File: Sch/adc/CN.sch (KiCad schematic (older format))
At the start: 19 parts, among them J1 JP4, J2 Header5, P1 CONN_02X40, U1 LTC2292

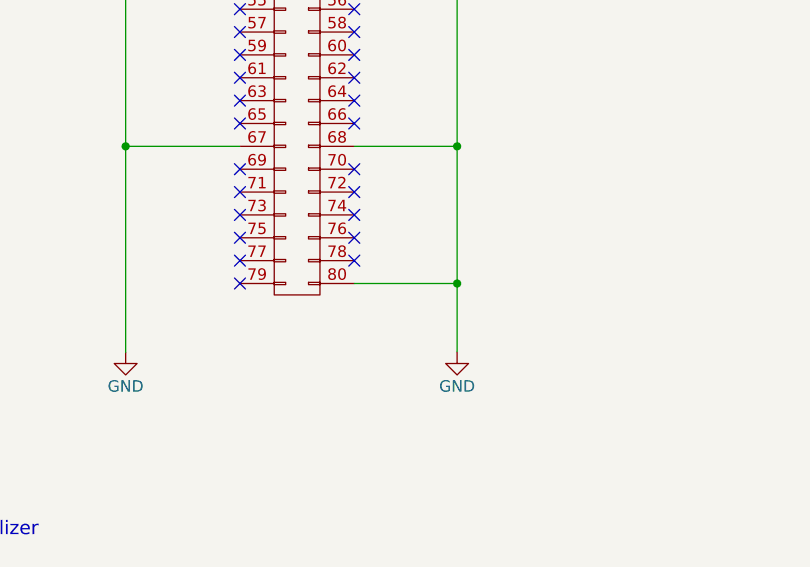
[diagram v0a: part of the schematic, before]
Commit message: Fixed GND short of pin 80
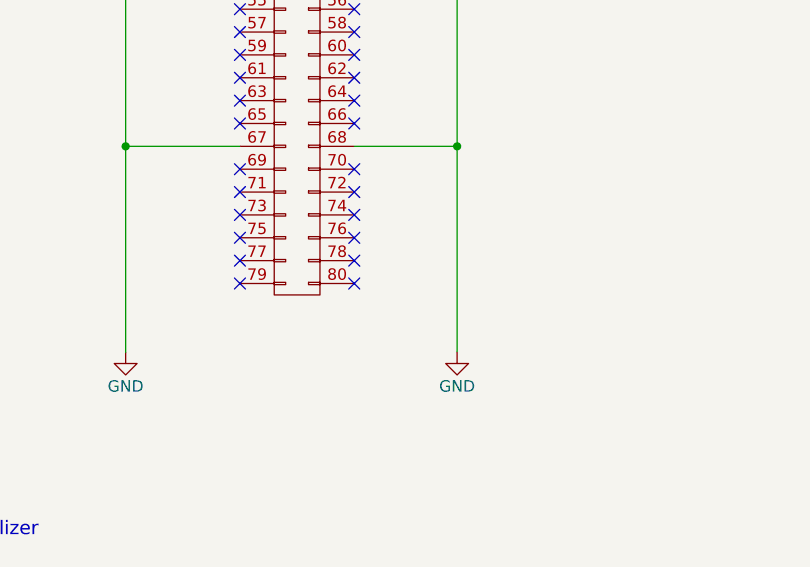
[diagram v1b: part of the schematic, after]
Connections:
- wire segments 147 -> 146
- no-connect marks 59 -> 60
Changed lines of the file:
@@
 Connection ~ 7600 1850
-Wire Wire Line
-	7150 5650 7600 5650
-Connection ~ 7600 5650
 Wire Wire Line
 	7150 2850 7600 2850
@@
 NoConn ~ 8350 2550
 NoConn ~ 5950 2550
+NoConn ~ 7150 5650
 $EndSCHEMATC

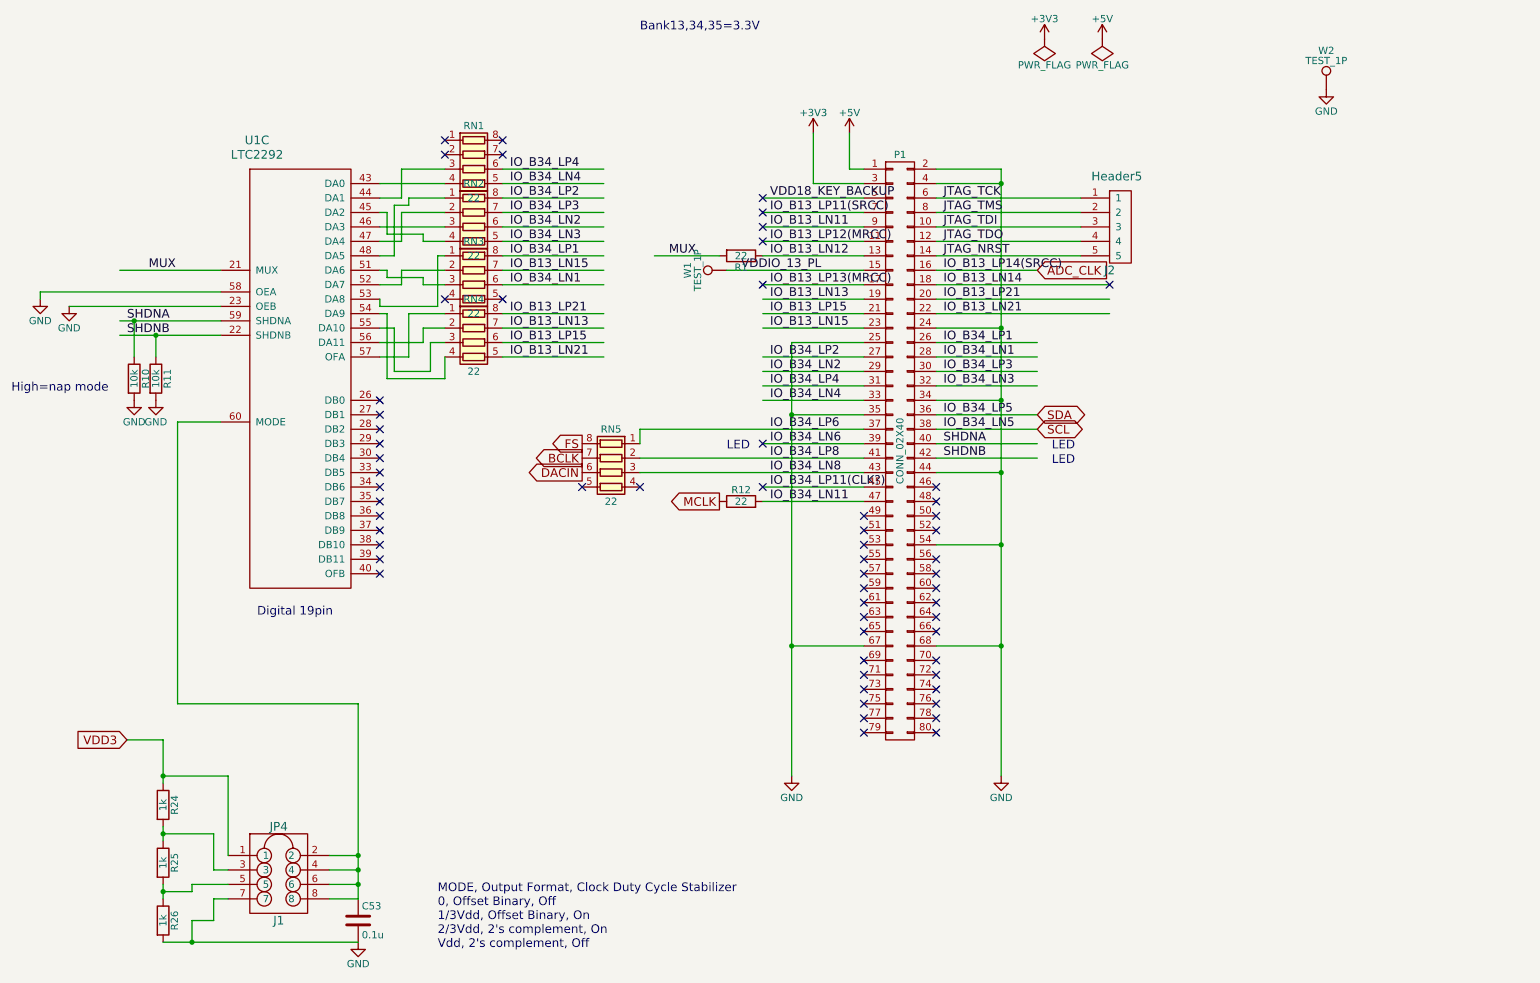
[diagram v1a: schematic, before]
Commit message: Modification in progress. Changed clock gen.
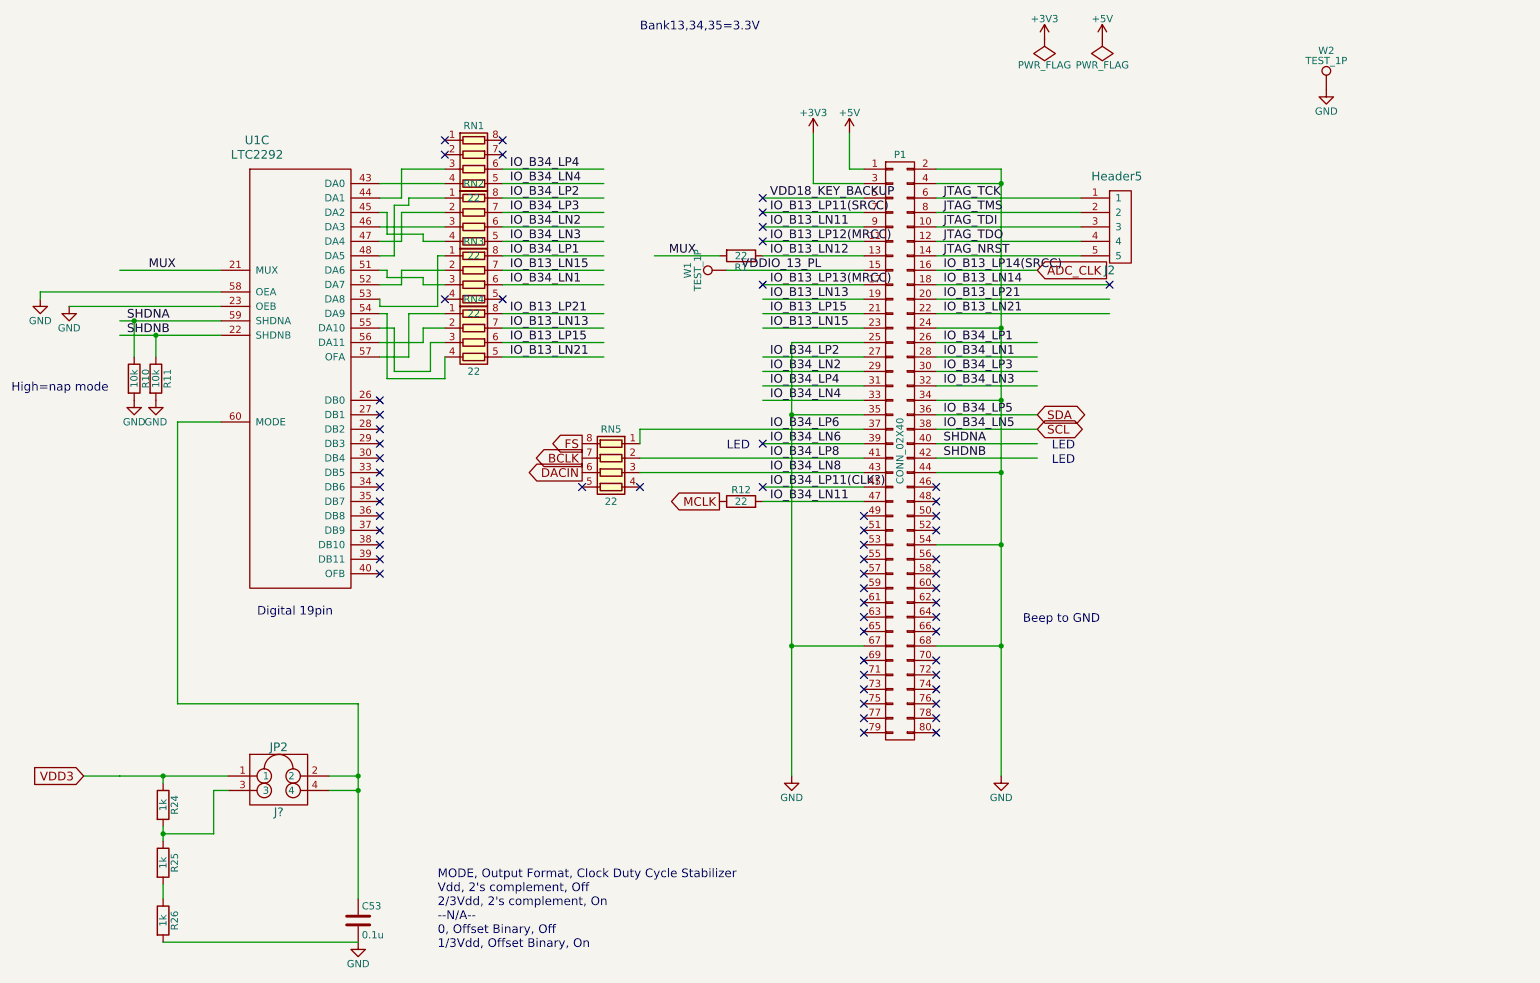
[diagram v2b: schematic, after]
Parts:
- removed J1: JP4, adc_lib:M20-9980445, symbol JP4
- added J?: JP2, symbol JP2
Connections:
- wire segments 146 -> 150
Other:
- note added: "Beep to GND"
- note added: "MODE, Output Format, Clock Duty Cycle Stabilizer\nVdd, 2's complement, Off\n2/3Vdd, 2's complement, On\n--N/A--\n0, Offset Binary, Off\n1/3Vdd, Offset Binary, On\n"
- note removed: "MODE, Output Format, Clock Duty Cycle Stabilizer\n0, Offset Binary, Off\n1/3Vdd, Offset Binary, On\n2/3Vdd, 2's complement, On\nVdd, 2's complement, Off"
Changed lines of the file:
@@
-	1    0    0    -1
-$EndComp
-$Comp
-L JP4 J1
-U 1 1 58A5FE9F
-P 2550 6650
-F 0 "J1" H 2600 6350 60  0000 C CNN
-F 1 "JP4" H 2600 7000 60  0000 C CNN
-F 2 "adc_lib:M20-9980445" H 2550 6900 60  0001 C CNN
-F 3 "" H 2550 6900 60  0001 C CNN
-	1    2550 6650
 	1    0    0    -1
 $EndComp
@@
 NoConn ~ 5950 3650
 Text Notes 3700 7150 0    60   ~ 0
-MODE, Output Format, Clock Duty Cycle Stabilizer\n0, Offset Binary, Off\n1/3Vdd, Offset Binary, On\n2/3Vdd, 2's complement, On\nVdd, 2's complement, Off
-Text GLabel 1550 5700 0    60   Input ~ 0
+MODE, Output Format, Clock Duty Cycle Stabilizer\nVdd, 2's complement, Off\n2/3Vdd, 2's complement, On\n--N/A--\n0, Offset Binary, Off\n1/3Vdd, Offset Binary, On\n
+Text GLabel 1250 5950 0    60   Input ~ 0
 VDD3
 $Comp
@@
 	7150 1750 7600 1750
 Wire Wire Line
-	7600 1750 7600 5950
+	7600 1750 7600 1850
+Wire Wire Line
+	7600 1850 7600 2850
+Wire Wire Line
+	7600 2850 7600 3350
+Wire Wire Line
+	7600 3350 7600 3850
+Wire Wire Line
+	7600 3850 7600 4350
+Wire Wire Line
+	7600 4350 7600 5050
+Wire Wire Line
+	7600 5050 7600 5950
 Wire Wire Line
 	7150 1850 7600 1850
@@
 	6150 5050 6650 5050
 Wire Wire Line
-	6150 2950 6150 5950
+	6150 2950 6150 3450
+Wire Wire Line
+	6150 3450 6150 5050
+Wire Wire Line
+	6150 5050 6150 5950
 Wire Wire Line
 	6650 3450 6150 3450
@@
 	950  2600 2200 2600
 Wire Wire Line
-	1500 2800 2200 2800
+	1500 2800 1600 2800
+Wire Wire Line
+	1600 2800 2200 2800
 Wire Wire Line
 	2200 2450 1500 2450
 Wire Wire Line
-	1800 5700 1800 6000
-Wire Wire Line
-	1800 6300 1800 6400
+	1500 5950 1800 5950
+Wire Wire Line
+	1800 5950 1800 6000
+Wire Wire Line
+	1800 6300 1800 6350
+Wire Wire Line
+	1800 6350 1800 6400
 Wire Wire Line
 	1800 6700 1800 6800
@@
 	1800 7100 3150 7100
 Wire Wire Line
-	3150 6800 2950 6800
-Wire Wire Line
-	3150 6700 2950 6700
-Wire Wire Line
-	3150 5450 3150 6800
-Wire Wire Line
-	2950 6600 3150 6600
-Connection ~ 3150 6700
-Wire Wire Line
-	2950 6500 3150 6500
-Connection ~ 3150 6600
+	3150 5450 3150 5950
+Wire Wire Line
+	3150 5950 3150 6050
+Wire Wire Line
+	3150 6050 3150 6800
 Wire Wire Line
 	1800 5950 2250 5950
-Wire Wire Line
-	2250 5950 2250 6500
 Connection ~ 1800 5950
 Wire Wire Line
 	1800 6350 2150 6350
-Wire Wire Line
-	2150 6350 2150 6600
-Wire Wire Line
-	2150 6600 2250 6600
 Connection ~ 1800 6350
 Wire Wire Line
-	1800 6750 2000 6750
-Wire Wire Line
-	2000 6750 2000 6700
-Wire Wire Line
-	2000 6700 2250 6700
-Connection ~ 1800 6750
-Wire Wire Line
-	2000 7100 2000 6950
-Wire Wire Line
-	2000 6950 2150 6950
-Wire Wire Line
-	2150 6950 2150 6800
-Wire Wire Line
-	2150 6800 2250 6800
-Connection ~ 2000 7100
-Wire Wire Line
 	2200 3500 1900 3500
 Wire Wire Line
@@
 Wire Wire Line
 	1900 5450 3150 5450
-Connection ~ 3150 6500
 Wire Wire Line
 	6650 2450 5700 2450
@@
 	7150 2250 8150 2250
 Wire Wire Line
-	1500 2900 2200 2900
+	1500 2900 1750 2900
+Wire Wire Line
+	1750 2900 2200 2900
 Wire Wire Line
 	1150 2700 2200 2700
 Wire Wire Line
-	1550 5700 1800 5700
+	1250 5950 1500 5950
 Wire Wire Line
 	950  2600 950  2650
@@
 NoConn ~ 5950 2550
 NoConn ~ 7150 5650
+Text Notes 7750 4900 0    60   ~ 0
+Beep to GND
+$Comp
+L JP2 J?
+U 1 1 594BFF08
+P 2600 5950
+F 0 "J?" H 2600 5700 60  0000 C CNN
+F 1 "JP2" H 2600 6150 60  0000 C CNN
+F 2 "" H 2550 6050 60  0001 C CNN
+F 3 "" H 2550 6050 60  0001 C CNN
+	1    2600 5950
+	1    0    0    -1
+$EndComp
+Wire Wire Line
+	2150 6350 2150 6050
+Wire Wire Line
+	2150 6050 2250 6050
+Wire Wire Line
+	2950 5950 3150 5950
+Connection ~ 3150 5950
+Wire Wire Line
+	2950 6050 3150 6050
+Connection ~ 3150 6050
 $EndSCHEMATC

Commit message: Changed PDS
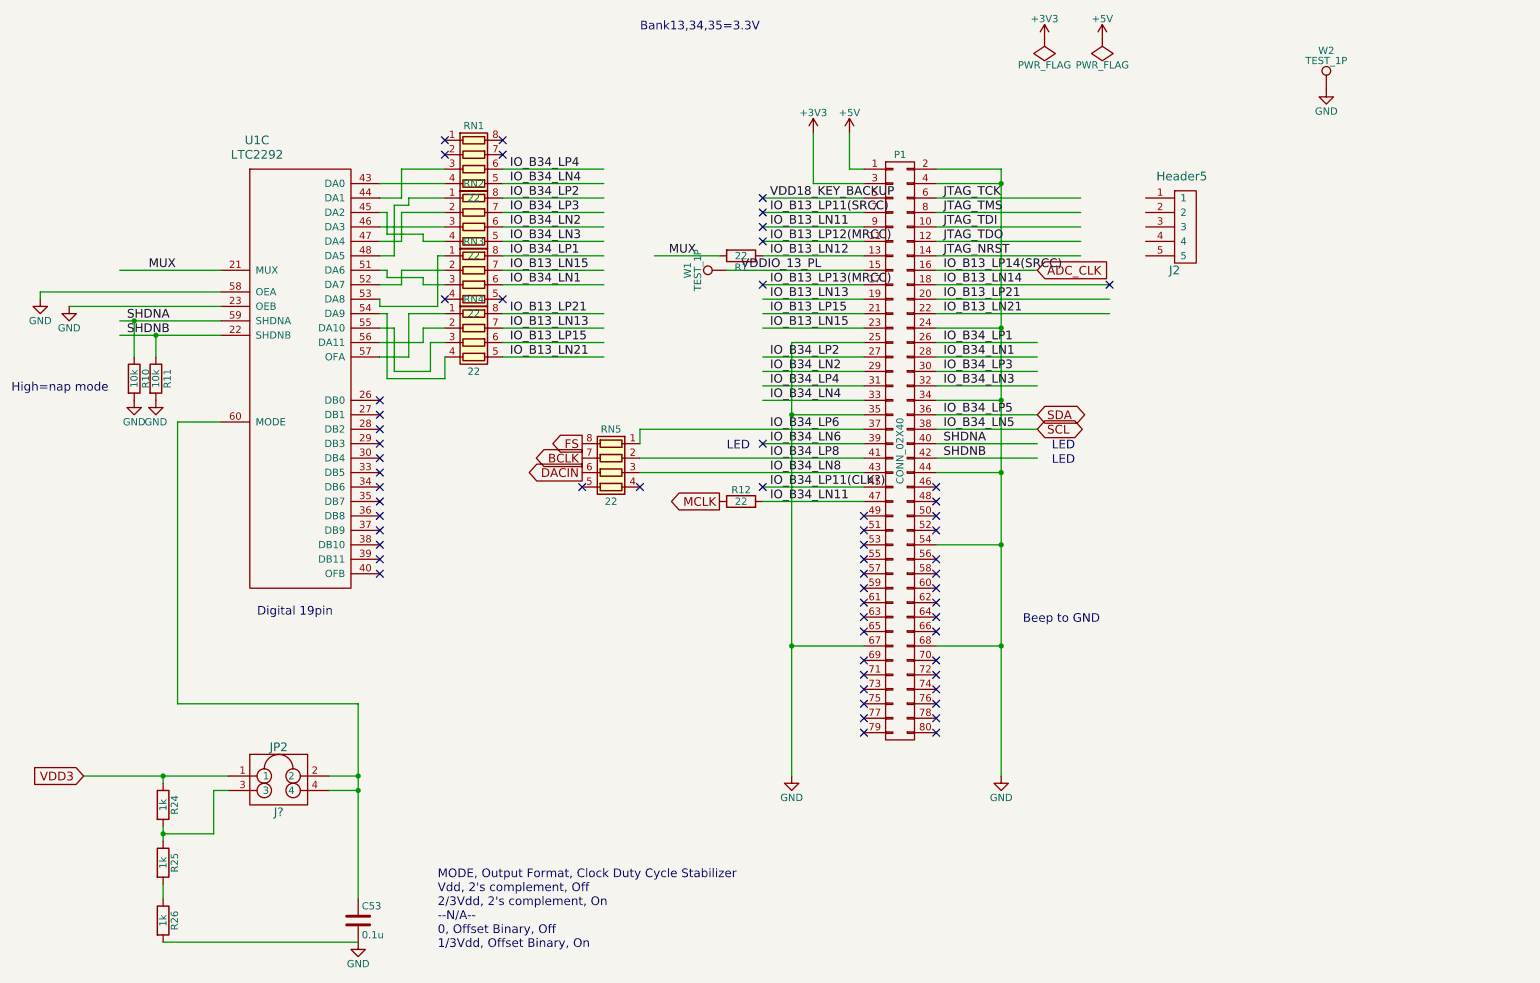
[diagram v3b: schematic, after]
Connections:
- wire segments 150 -> 135
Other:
- moved on the sheet: J2
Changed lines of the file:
@@
 L Header5 J2
 U 1 1 58A52616
-P 8350 2150
-F 0 "J2" H 8350 1850 60  0000 C CNN
-F 1 "Header5" H 8400 2500 60  0000 C CNN
-F 2 "adc_lib:M20-9990546" H 8350 2250 60  0001 C CNN
-F 3 "" H 8350 2250 60  0001 C CNN
-	1    8350 2150
+P 8800 2150
+F 0 "J2" H 8800 1850 60  0000 C CNN
+F 1 "Header5" H 8850 2500 60  0000 C CNN
+F 2 "adc_lib:M20-9990546" H 8800 2250 60  0001 C CNN
+F 3 "" H 8800 2250 60  0001 C CNN
+	1    8800 2150
 	1    0    0    -1
 $EndComp
@@
 	7150 1750 7600 1750
 Wire Wire Line
-	7600 1750 7600 1850
-Wire Wire Line
-	7600 1850 7600 2850
-Wire Wire Line
-	7600 2850 7600 3350
-Wire Wire Line
-	7600 3350 7600 3850
-Wire Wire Line
-	7600 3850 7600 4350
-Wire Wire Line
-	7600 4350 7600 5050
-Wire Wire Line
-	7600 5050 7600 5950
+	7600 1750 7600 5950
 Wire Wire Line
 	7150 1850 7600 1850
@@
 	6150 5050 6650 5050
 Wire Wire Line
-	6150 2950 6150 3450
-Wire Wire Line
-	6150 3450 6150 5050
-Wire Wire Line
-	6150 5050 6150 5950
+	6150 2950 6150 5950
 Wire Wire Line
 	6650 3450 6150 3450
@@
 	950  2600 2200 2600
 Wire Wire Line
-	1500 2800 1600 2800
-Wire Wire Line
-	1600 2800 2200 2800
+	1500 2800 2200 2800
 Wire Wire Line
 	2200 2450 1500 2450
 Wire Wire Line
-	1500 5950 1800 5950
+	1250 5950 2250 5950
 Wire Wire Line
 	1800 5950 1800 6000
 Wire Wire Line
-	1800 6300 1800 6350
-Wire Wire Line
-	1800 6350 1800 6400
+	1800 6300 1800 6400
 Wire Wire Line
 	1800 6700 1800 6800
@@
 	1800 7100 3150 7100
 Wire Wire Line
-	3150 5450 3150 5950
-Wire Wire Line
-	3150 5950 3150 6050
-Wire Wire Line
-	3150 6050 3150 6800
-Wire Wire Line
-	1800 5950 2250 5950
+	3150 5450 3150 6800
 Connection ~ 1800 5950
 Wire Wire Line
@@
 	7150 2250 8150 2250
 Wire Wire Line
-	1500 2900 1750 2900
-Wire Wire Line
-	1750 2900 2200 2900
+	1500 2900 2200 2900
 Wire Wire Line
 	1150 2700 2200 2700
 Wire Wire Line
-	1250 5950 1500 5950
-Wire Wire Line
 	950  2600 950  2650
